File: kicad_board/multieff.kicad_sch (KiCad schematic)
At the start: 39 parts, among them J1 Wha1, U1 MCP23017_SO, U2 MCP23017_SO, U4 ADS1115IDGS

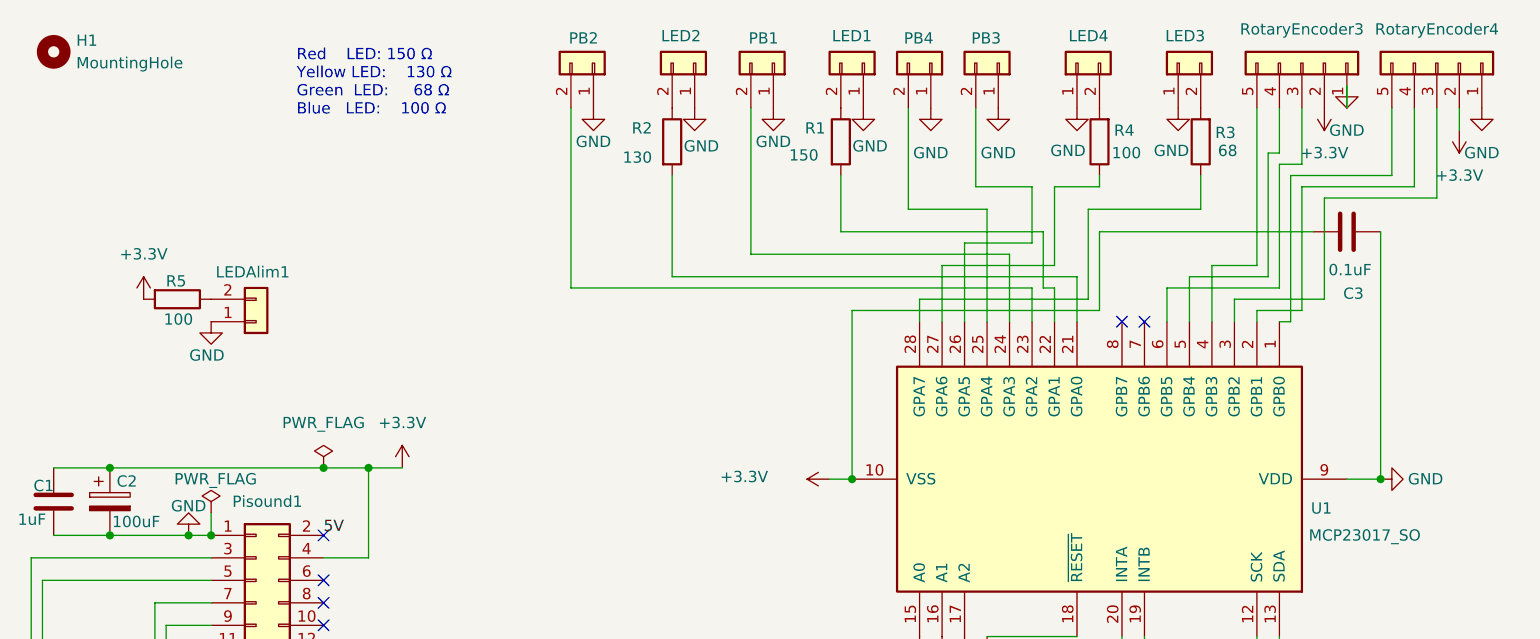
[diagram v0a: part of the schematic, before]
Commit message: Add decoupling capacitors to LEDs
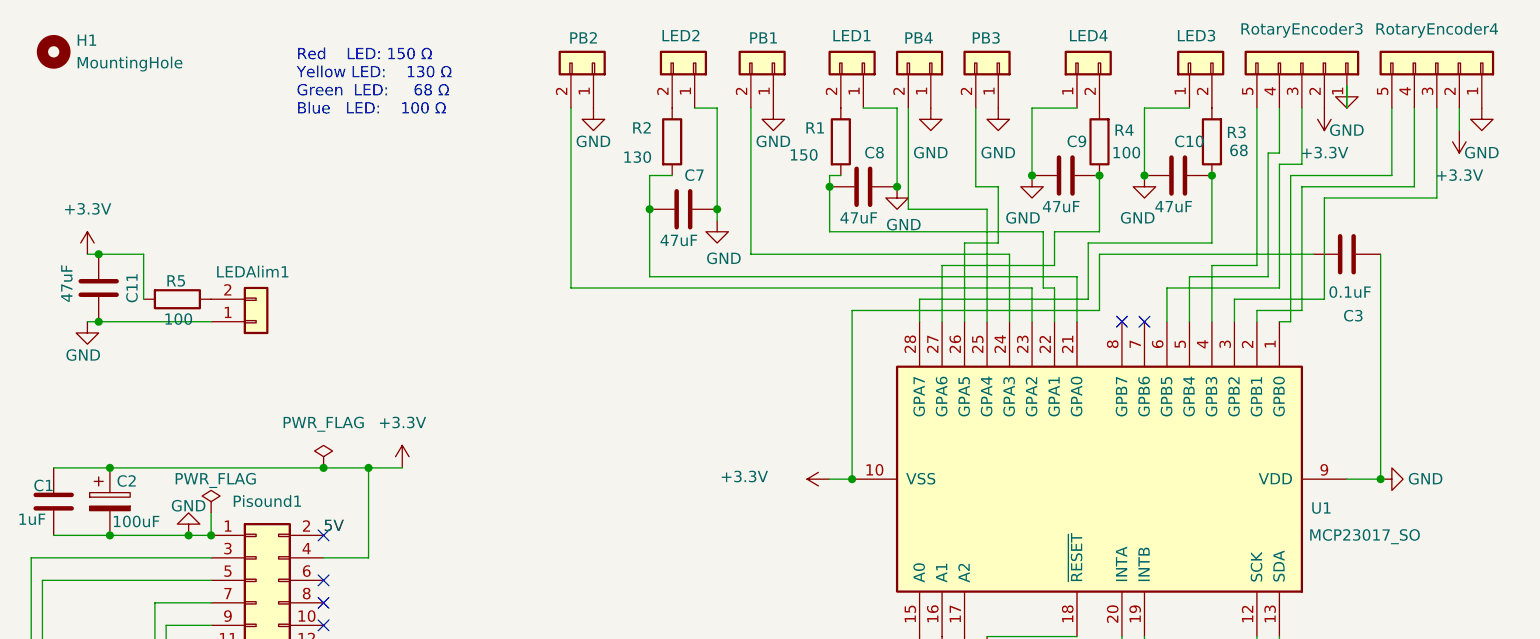
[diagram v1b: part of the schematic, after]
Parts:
- added C10, C11, C7, C8, C9: 47uF, PCM_Capacitor_SMD_AKL:C_0805_2012Metric, symbol PCM_Capacitor_AKL:C_0805
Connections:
- net +3.3V: now also C11.1
- net GND: now also C10.1, C11.2, C7.2, C8.2, C9.1
- net at R2.2, U1.21 (GPA0): now also C7.1
- net at R4.1, U1.27 (GPA6): now also C9.2
- net at R1.2, U1.22 (GPA1): now also C8.1
- net at R3.1, U1.28 (GPA7): now also C10.2
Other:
- moved on the sheet: C3, LED3, R3

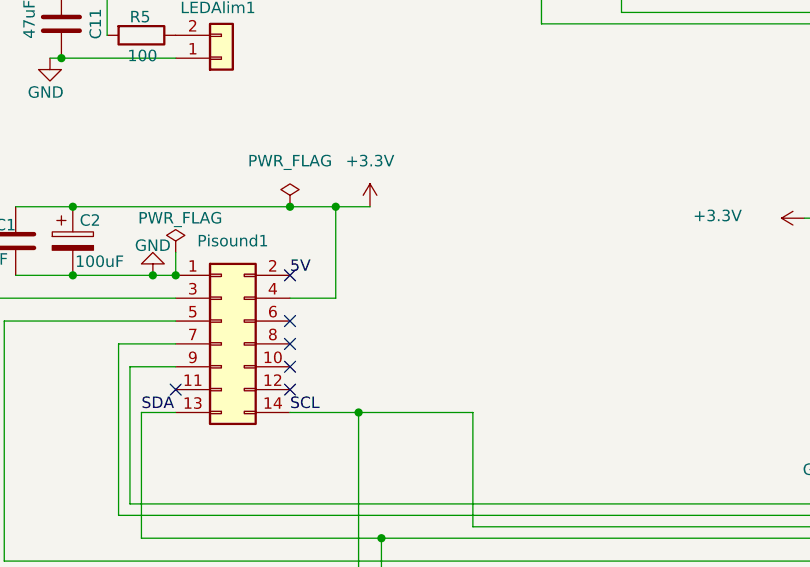
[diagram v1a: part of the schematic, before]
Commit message: Add missing screen alim connector
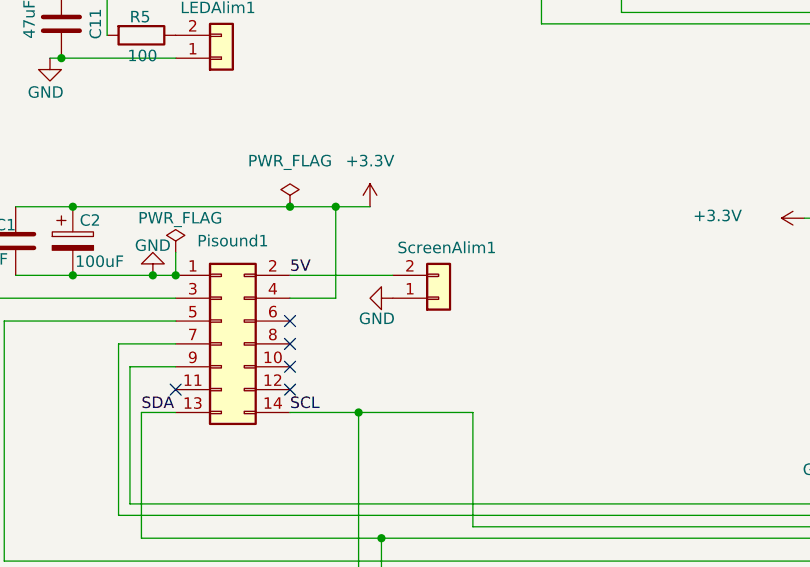
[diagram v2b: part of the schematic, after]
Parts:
- added ScreenAlim1: Conn_01x02, Connector_JST:JST_XH_B2B-XH-AM_1x02_P2.50mm_Vertical, symbol Connector_Generic:Conn_01x02
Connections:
- net 5V: now also ScreenAlim1.2 (Pin_2)
- net GND: now also ScreenAlim1.1 (Pin_1)
- no-connect marks 10 -> 9
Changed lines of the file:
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@@
 	)
 	(no_connect
-		(at 48.26 72.39)
-	)
-	(no_connect
 		(at 138.43 163.83)
 	)
@@
 	(wire
 		(pts
+			(xy 48.26 72.39) (xy 59.69 72.39)
+		)
+		(stroke
+			(width 0)
+			(type default)
+		)
+	)
+	(wire
+		(pts
 			(xy 130.81 44.45) (xy 129.54 44.45)
 		)
@@
 	)
 	(symbol
+		(lib_id "Connector_Generic:Conn_01x02")
+		(at 64.77 74.93 0)
+		(mirror x)
+		(unit 1)
+		(exclude_from_sim no)
+		(in_bom yes)
+		(on_board yes)
+		(dnp no)
+		(property "Reference" "ScreenAlim1"
+			(at 60.198 69.342 0)
+			(effects
+				(font
+					(size 1.27 1.27)
+				)
+				(justify left)
+			)
+		)
+		(property "Value" "Conn_01x02"
+			(at 67.31 72.3901 0)
+			(effects
+				(font
+					(size 1.27 1.27)
+				)
+				(justify left)
+				(hide yes)
+			)
+		)
+		(property "Footprint" "Connector_JST:JST_XH_B2B-XH-AM_1x02_P2.50mm_Vertical"
+			(at 64.77 74.93 0)
+			(effects
+				(font
+					(size 1.27 1.27)
+				)
+				(hide yes)
+			)
+		)
+		(property "Datasheet" "~"
+			(at 64.77 74.93 0)
+			(effects
+				(font
+					(size 1.27 1.27)
+				)
+				(hide yes)
+			)
+		)
+		(property "Description" "Generic connector, single row, 01x02, script generated (kicad-library-utils/schlib/autogen/connector/)"
+			(at 64.77 74.93 0)
+			(effects
+				(font
+					(size 1.27 1.27)
+				)
+				(hide yes)
+			)
+		)
+		(pin "1"
+		)
+		(pin "2"
+		)
+		(instances
+			(project "multieff"
+				(path "/01a67eee-3893-4e68-bed0-a04a64951ab4"
+					(reference "ScreenAlim1")
+					(unit 1)
+				)
+			)
+		)
+	)
+	(symbol
 		(lib_id "PCM_Resistor_AKL:R_0612")
 		(at 41.91 114.3 90)
@@
 					(unit 1)
 				)
+			)
+		)
+	)
+	(symbol
+		(lib_id "power:GND")
+		(at 59.69 74.93 270)
+		(mirror x)
+		(unit 1)
+		(exclude_from_sim no)
+		(in_bom yes)
+		(on_board yes)
+		(dnp no)
+		(property "Reference" "#PWR07"
+			(at 53.34 74.93 0)
+			(effects
+				(font
+					(size 1.27 1.27)
+				)
+				(hide yes)
+			)
+		)
+		(property "Value" "GND"
+			(at 57.912 77.216 90)
+			(effects
+				(font
+					(size 1.27 1.27)
+				)
+			)
+		)
+		(property "Footprint" ""
+			(at 59.69 74.93 0)
+			(effects
+				(font
+					(size 1.27 1.27)
+				)
+				(hide yes)
+			)
+		)
+		(property "Datasheet" ""
+			(at 59.69 74.93 0)
+			(effects
+				(font
+					(size 1.27 1.27)
+				)
+				(hide yes)
+			)
+		)
+		(property "Description" "Power symbol creates a global label with name \"GND\" , ground"
+			(at 59.69 74.93 0)
+			(effects
+				(font
+					(size 1.27 1.27)
+				)
+				(hide yes)
+			)
+		)
+		(pin "1"
+		)
+		(instances
+			(project "multieff"
+				(path "/01a67eee-3893-4e68-bed0-a04a64951ab4"
+					(reference "#PWR07")
+					(unit 1)
+				)
